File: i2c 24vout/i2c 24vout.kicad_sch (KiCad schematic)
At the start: 73 parts, among them J1 power in, J2 Conn_01x04, J3 Conn_01x04, J4 Conn_01x04, J5 Conn_01x04, J6 to qwiic breakout, U1 ILQ620GB-X009, U2 ILQ620GB-X009, U3 ILQ620GB-X009, U4 ILQ620GB-X009, U5 PCA9685PW

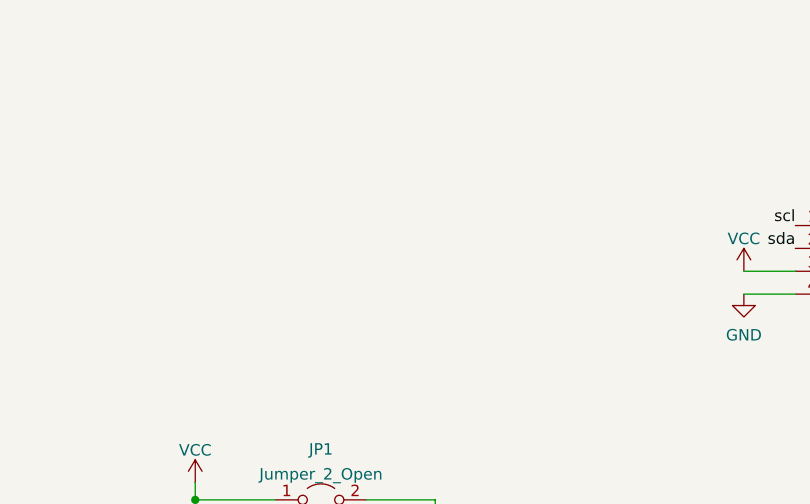
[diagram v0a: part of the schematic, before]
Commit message: added qwiic connectors to boards as well as breakout connector
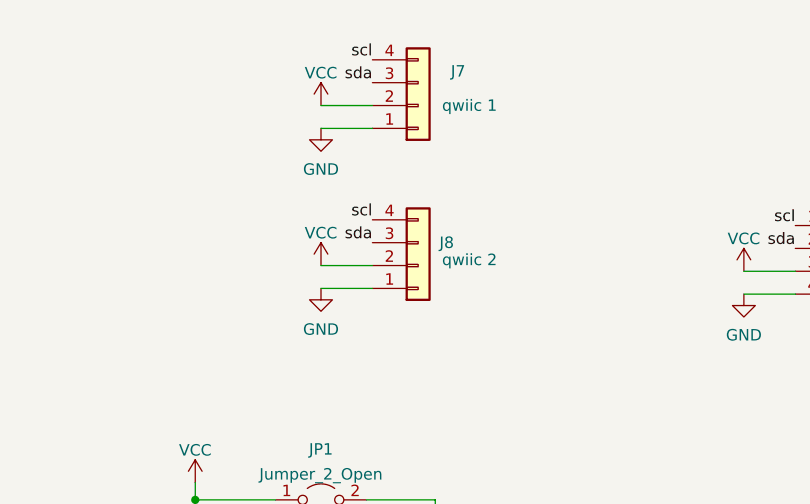
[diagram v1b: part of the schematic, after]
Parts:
- added J7: qwiic 1, Connector_JST:JST_SH_SM04B-SRSS-TB_1x04-1MP_P1.00mm_Horizontal, symbol Connector_Generic:Conn_01x04
- added J8: qwiic 2, Connector_JST:JST_SH_SM04B-SRSS-TB_1x04-1MP_P1.00mm_Horizontal, symbol Connector_Generic:Conn_01x04
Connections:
- net GND: now also J7.1 (Pin_1), J8.1 (Pin_1)
- net VCC: now also J7.2 (Pin_2), J8.2 (Pin_2)
- net scl: now also J7.4 (Pin_4), J8.4 (Pin_4)
- net sda: now also J7.3 (Pin_3), J8.3 (Pin_3)
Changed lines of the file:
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@@
+    (stroke (width 0) (type default) (color 0 0 0 0))
+  )
+  (wire (pts (xy 154.305 25.4) (xy 160.02 25.4))
     (stroke (width 0) (type default) (color 0 0 0 0))
   )
@@
     (stroke (width 0) (type default) (color 0 0 0 0))
   )
+  (wire (pts (xy 154.305 43.18) (xy 160.02 43.18))
+    (stroke (width 0) (type default) (color 0 0 0 0))
+  )
   (wire (pts (xy 60.96 79.375) (xy 71.755 79.375))
     (stroke (width 0) (type default) (color 0 0 0 0))
@@
     (stroke (width 0) (type default) (color 0 0 0 0))
   )
+  (wire (pts (xy 154.305 40.64) (xy 160.02 40.64))
+    (stroke (width 0) (type default) (color 0 0 0 0))
+  )
   (wire (pts (xy 60.96 69.215) (xy 71.755 69.215))
     (stroke (width 0) (type default) (color 0 0 0 0))
@@
   )
   (wire (pts (xy 56.515 97.155) (xy 56.515 107.315))
+    (stroke (width 0) (type default) (color 0 0 0 0))
+  )
+  (wire (pts (xy 154.305 22.86) (xy 160.02 22.86))
     (stroke (width 0) (type default) (color 0 0 0 0))
   )
@@
     (effects (font (size 1.27 1.27)) (justify right bottom))
   )
+  (label "sda" (at 160.02 20.32 180)
+    (effects (font (size 1.27 1.27)) (justify right bottom))
+  )
   (label "pwm12" (at 263.525 78.105 0)
     (effects (font (size 1.27 1.27)) (justify left bottom))
@@
     (effects (font (size 1.27 1.27)) (justify right bottom))
   )
+  (label "scl" (at 160.02 35.56 180)
+    (effects (font (size 1.27 1.27)) (justify right bottom))
+  )
   (label "pwm5" (at 23.495 76.835 180)
     (effects (font (size 1.27 1.27)) (justify right bottom))
@@
     (effects (font (size 1.27 1.27)) (justify right bottom))
   )
+  (label "sda" (at 160.02 38.1 180)
+    (effects (font (size 1.27 1.27)) (justify right bottom))
+  )
   (label "pwm14" (at 23.495 168.275 180)
     (effects (font (size 1.27 1.27)) (justify right bottom))
@@
   )
   (label "pwm1" (at 23.495 36.195 180)
+    (effects (font (size 1.27 1.27)) (justify right bottom))
+  )
+  (label "scl" (at 160.02 17.78 180)
     (effects (font (size 1.27 1.27)) (justify right bottom))
   )
@@
     (pin "3")
     (pin "4")
+  )
+  (symbol (lib_id "power:GND") (at 154.305 43.18 0) (unit 1)
+    (in_bom yes) (on_board yes) (fields_autoplaced)
+    (property "Reference" "#PWR04" (id 0) (at 154.305 49.53 0)
+      (effects (font (size 1.27 1.27)) hide)
+    )
+    (property "Value" "GND" (id 1) (at 154.305 47.7425 0))
+    (property "Footprint" "" (id 2) (at 154.305 43.18 0)
+      (effects (font (size 1.27 1.27)) hide)
+    )
+    (property "Datasheet" "" (id 3) (at 154.305 43.18 0)
+      (effects (font (size 1.27 1.27)) hide)
+    )
+    (pin "1")
   )
   (symbol (lib_id "Evan's misc parts:ILQ620GB-X009") (at 42.545 99.695 0) (unit 1)
@@
     (pin "2")
   )
+  (symbol (lib_id "power:GND") (at 154.305 25.4 0) (unit 1)
+    (in_bom yes) (on_board yes) (fields_autoplaced)
+    (property "Reference" "#PWR02" (id 0) (at 154.305 31.75 0)
+      (effects (font (size 1.27 1.27)) hide)
+    )
+    (property "Value" "GND" (id 1) (at 154.305 29.9625 0))
+    (property "Footprint" "" (id 2) (at 154.305 25.4 0)
+      (effects (font (size 1.27 1.27)) hide)
+    )
+    (property "Datasheet" "" (id 3) (at 154.305 25.4 0)
+      (effects (font (size 1.27 1.27)) hide)
+    )
+    (pin "1")
+  )
   (symbol (lib_id "Device:R") (at 27.305 26.035 270) (unit 1)
     (in_bom yes) (on_board yes) (fields_autoplaced)
@@
     (pin "2")
   )
+  (symbol (lib_id "power:VCC") (at 154.305 40.64 0) (unit 1)
+    (in_bom yes) (on_board yes) (fields_autoplaced)
+    (property "Reference" "#PWR03" (id 0) (at 154.305 44.45 0)
+      (effects (font (size 1.27 1.27)) hide)
+    )
+    (property "Value" "VCC" (id 1) (at 154.305 37.0355 0))
+    (property "Footprint" "" (id 2) (at 154.305 40.64 0)
+      (effects (font (size 1.27 1.27)) hide)
+    )
+    (property "Datasheet" "" (id 3) (at 154.305 40.64 0)
+      (effects (font (size 1.27 1.27)) hide)
+    )
+    (pin "1")
+  )
   (symbol (lib_id "Device:R") (at 27.305 66.675 270) (unit 1)
     (in_bom yes) (on_board yes) (fields_autoplaced)
@@
     (pin "1")
   )
+  (symbol (lib_id "Connector_Generic:Conn_01x04") (at 165.1 40.64 0) (mirror x) (unit 1)
+    (in_bom yes) (on_board yes)
+    (property "Reference" "J8" (id 0) (at 168.275 38.1 0))
+    (property "Value" "qwiic 2" (id 1) (at 170.815 40.005 0))
+    (property "Footprint" "Connector_JST:JST_SH_SM04B-SRSS-TB_1x04-1MP_P1.00mm_Horizontal" (id 2) (at 165.1 40.64 0)
+      (effects (font (size 1.27 1.27)) hide)
+    )
+    (property "Datasheet" "~" (id 3) (at 165.1 40.64 0)
+      (effects (font (size 1.27 1.27)) hide)
+    )
+    (pin "1")
+    (pin "2")
+    (pin "3")
+    (pin "4")
+  )
   (symbol (lib_id "power:+24V") (at 56.515 19.685 0) (unit 1)
     (in_bom yes) (on_board yes) (fields_autoplaced)
@@
     (pin "1")
     (pin "2")
+  )
+  (symbol (lib_id "power:VCC") (at 154.305 22.86 0) (unit 1)
+    (in_bom yes) (on_board yes) (fields_autoplaced)
+    (property "Reference" "#PWR01" (id 0) (at 154.305 26.67 0)
+      (effects (font (size 1.27 1.27)) hide)
+    )
+    (property "Value" "VCC" (id 1) (at 154.305 19.2555 0))
+    (property "Footprint" "" (id 2) (at 154.305 22.86 0)
+      (effects (font (size 1.27 1.27)) hide)
+    )
+    (property "Datasheet" "" (id 3) (at 154.305 22.86 0)
+      (effects (font (size 1.27 1.27)) hide)
+    )
+    (pin "1")
   )
   (symbol (lib_id "Device:C") (at 60.96 65.405 0) (unit 1)
@@
     (pin "2")
   )
+  (symbol (lib_id "Connector_Generic:Conn_01x04") (at 165.1 22.86 0) (mirror x) (unit 1)
+    (in_bom yes) (on_board yes)
+    (property "Reference" "J7" (id 0) (at 169.545 19.05 0))
+    (property "Value" "qwiic 1" (id 1) (at 170.815 22.86 0))
+    (property "Footprint" "Connector_JST:JST_SH_SM04B-SRSS-TB_1x04-1MP_P1.00mm_Horizontal" (id 2) (at 165.1 22.86 0)
+      (effects (font (size 1.27 1.27)) hide)
+    )
+    (property "Datasheet" "~" (id 3) (at 165.1 22.86 0)
+      (effects (font (size 1.27 1.27)) hide)
+    )
+    (pin "1")
+    (pin "2")
+    (pin "3")
+    (pin "4")
+  )
   (symbol (lib_id "Device:R") (at 71.755 45.085 0) (unit 1)
     (in_bom yes) (on_board yes) (fields_autoplaced)
@@
   )
   (symbol_instances
+    (path "/b71aee81-8ccc-488b-87a3-550495135d8e"
+      (reference "#PWR01") (unit 1) (value "VCC") (footprint "")
+    )
+    (path "/4175c327-a7fe-4d84-ba69-9ba6e02c58fb"
+      (reference "#PWR02") (unit 1) (value "GND") (footprint "")
+    )
+    (path "/52ec8b76-9d1a-4183-bd6e-a535fa00310c"
+      (reference "#PWR03") (unit 1) (value "VCC") (footprint "")
+    )
+    (path "/12f5ec82-4dbe-408e-aaae-0e3618d856e5"
+      (reference "#PWR04") (unit 1) (value "GND") (footprint "")
+    )
     (path "/653b3b7f-63b7-4063-8482-5cb2e6bca5d9"
       (reference "#PWR0101") (unit 1) (value "GND") (footprint "")
@@
       (reference "J6") (unit 1) (value "to qwiic breakout") (footprint "Connector_PinHeader_2.54mm:PinHeader_1x04_P2.54mm_Vertical")
     )
+    (path "/e8cfcc49-0e38-439d-bb8a-686b576038c2"
+      (reference "J7") (unit 1) (value "qwiic 1") (footprint "Connector_JST:JST_SH_SM04B-SRSS-TB_1x04-1MP_P1.00mm_Horizontal")
+    )
+    (path "/9a77615a-bb77-4b24-9f7e-2a282758ce30"
+      (reference "J8") (unit 1) (value "qwiic 2") (footprint "Connector_JST:JST_SH_SM04B-SRSS-TB_1x04-1MP_P1.00mm_Horizontal")
+    )
     (path "/f620a1b7-aab5-4053-912e-f514c747583a"

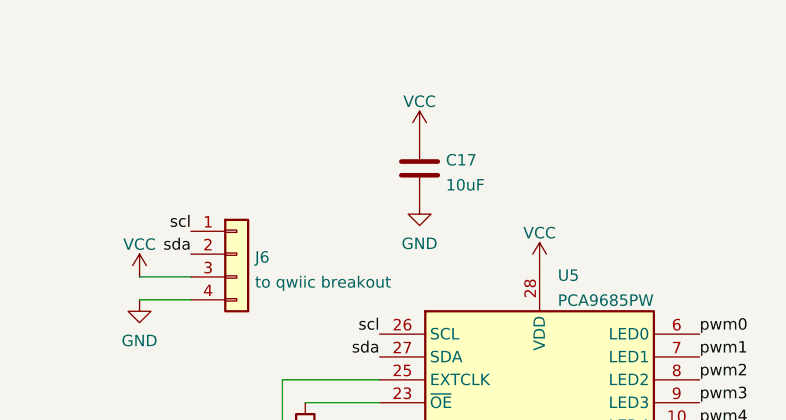
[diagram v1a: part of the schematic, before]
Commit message: reel detent added
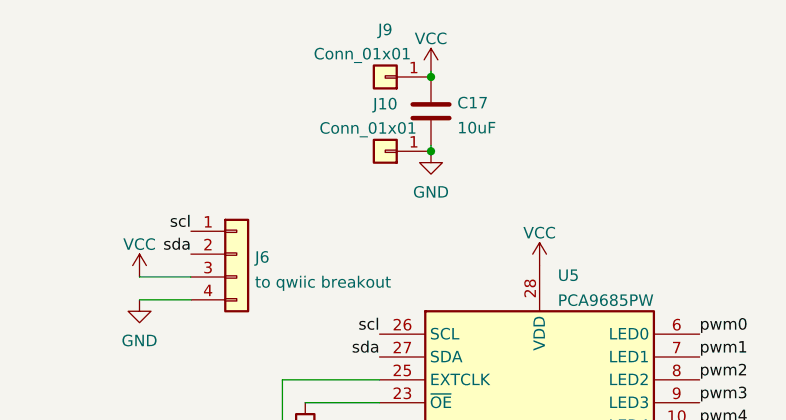
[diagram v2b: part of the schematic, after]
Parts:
- added J10, J9: Conn_01x01, Connector_PinHeader_2.54mm:PinHeader_1x01_P2.54mm_Vertical, symbol Connector_Generic:Conn_01x01
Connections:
- net GND: now also J10.1 (Pin_1)
- net VCC: now also J9.1 (Pin_1)
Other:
- moved on the sheet: C17
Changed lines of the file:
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@@
   (junction (at 33.02 41.275) (diameter 0) (color 0 0 0 0)
   )
+  (junction (at 233.68 27.305) (diameter 0) (color 0 0 0 0)
+  )
   (junction (at 78.105 150.495) (diameter 0) (color 0 0 0 0)
   )
@@
   (junction (at 187.96 121.285) (diameter 0) (color 0 0 0 0)
   )
+  (junction (at 233.68 19.05) (diameter 0) (color 0 0 0 0)
+  )
   (junction (at 56.515 168.275) (diameter 0) (color 0 0 0 0)
   )
@@
     (stroke (width 0) (type default) (color 0 0 0 0))
   )
+  (wire (pts (xy 233.68 27.305) (xy 233.68 26.67))
+    (stroke (width 0) (type default) (color 0 0 0 0))
+  )
   (wire (pts (xy 71.755 150.495) (xy 78.105 150.495))
     (stroke (width 0) (type default) (color 0 0 0 0))
@@
   )
   (wire (pts (xy 159.385 92.71) (xy 187.96 92.71))
+    (stroke (width 0) (type default) (color 0 0 0 0))
+  )
+  (wire (pts (xy 233.68 18.415) (xy 233.68 19.05))
     (stroke (width 0) (type default) (color 0 0 0 0))
   )
@@
     (pin "16")
     (pin "2")
+  )
+  (symbol (lib_id "Connector_Generic:Conn_01x01") (at 228.6 27.305 180) (unit 1)
+    (in_bom yes) (on_board yes)
+    (property "Reference" "J10" (id 0) (at 228.6 22.0685 0))
+    (property "Value" "Conn_01x01" (id 1) (at 226.695 24.765 0))
+    (property "Footprint" "Connector_PinHeader_2.54mm:PinHeader_1x01_P2.54mm_Vertical" (id 2) (at 228.6 27.305 0)
+      (effects (font (size 1.27 1.27)) hide)
+    )
+    (property "Datasheet" "~" (id 3) (at 228.6 27.305 0)
+      (effects (font (size 1.27 1.27)) hide)
+    )
+    (pin "1")
   )
   (symbol (lib_id "Device:R") (at 27.305 86.995 270) (unit 1)
@@
     (pin "1")
   )
-  (symbol (lib_id "power:VCC") (at 232.41 25.4 0) (unit 1)
-    (in_bom yes) (on_board yes) (fields_autoplaced)
-    (property "Reference" "#PWR0112" (id 0) (at 232.41 29.21 0)
-      (effects (font (size 1.27 1.27)) hide)
-    )
-    (property "Value" "VCC" (id 1) (at 232.41 21.7955 0))
-    (property "Footprint" "" (id 2) (at 232.41 25.4 0)
-      (effects (font (size 1.27 1.27)) hide)
-    )
-    (property "Datasheet" "" (id 3) (at 232.41 25.4 0)
+  (symbol (lib_id "power:VCC") (at 233.68 18.415 0) (unit 1)
+    (in_bom yes) (on_board yes) (fields_autoplaced)
+    (property "Reference" "#PWR0112" (id 0) (at 233.68 22.225 0)
+      (effects (font (size 1.27 1.27)) hide)
+    )
+    (property "Value" "VCC" (id 1) (at 233.68 14.8105 0))
+    (property "Footprint" "" (id 2) (at 233.68 18.415 0)
+      (effects (font (size 1.27 1.27)) hide)
+    )
+    (property "Datasheet" "" (id 3) (at 233.68 18.415 0)
       (effects (font (size 1.27 1.27)) hide)
     )
@@
     (pin "2")
   )
-  (symbol (lib_id "Device:C") (at 232.41 29.21 0) (unit 1)
-    (in_bom yes) (on_board yes) (fields_autoplaced)
-    (property "Reference" "C17" (id 0) (at 235.331 28.3015 0)
-      (effects (font (size 1.27 1.27)) (justify left))
-    )
-    (property "Value" "10uF" (id 1) (at 235.331 31.0766 0)
-      (effects (font (size 1.27 1.27)) (justify left))
-    )
-    (property "Footprint" "Capacitor_SMD:C_0603_1608Metric" (id 2) (at 233.3752 33.02 0)
-      (effects (font (size 1.27 1.27)) hide)
-    )
-    (property "Datasheet" "~" (id 3) (at 232.41 29.21 0)
+  (symbol (lib_id "Device:C") (at 233.68 22.86 0) (unit 1)
+    (in_bom yes) (on_board yes) (fields_autoplaced)
+    (property "Reference" "C17" (id 0) (at 236.601 21.9515 0)
+      (effects (font (size 1.27 1.27)) (justify left))
+    )
+    (property "Value" "10uF" (id 1) (at 236.601 24.7266 0)
+      (effects (font (size 1.27 1.27)) (justify left))
+    )
+    (property "Footprint" "Capacitor_SMD:C_0603_1608Metric" (id 2) (at 234.6452 26.67 0)
+      (effects (font (size 1.27 1.27)) hide)
+    )
+    (property "Datasheet" "~" (id 3) (at 233.68 22.86 0)
       (effects (font (size 1.27 1.27)) hide)
     )
@@
     (pin "2")
   )
+  (symbol (lib_id "Connector_Generic:Conn_01x01") (at 228.6 19.05 180) (unit 1)
+    (in_bom yes) (on_board yes)
+    (property "Reference" "J9" (id 0) (at 228.6 13.8135 0))
+    (property "Value" "Conn_01x01" (id 1) (at 226.06 16.51 0))
+    (property "Footprint" "Connector_PinHeader_2.54mm:PinHeader_1x01_P2.54mm_Vertical" (id 2) (at 228.6 19.05 0)
+      (effects (font (size 1.27 1.27)) hide)
+    )
+    (property "Datasheet" "~" (id 3) (at 228.6 19.05 0)
+      (effects (font (size 1.27 1.27)) hide)
+    )
+    (pin "1")
+  )
   (symbol (lib_id "power:VCC") (at 245.745 40.005 0) (unit 1)
     (in_bom yes) (on_board yes) (fields_autoplaced)
@@
     (pin "9")
   )
-  (symbol (lib_id "power:GND") (at 232.41 33.02 0) (unit 1)
-    (in_bom yes) (on_board yes) (fields_autoplaced)
-    (property "Reference" "#PWR0113" (id 0) (at 232.41 39.37 0)
-      (effects (font (size 1.27 1.27)) hide)
-    )
-    (property "Value" "GND" (id 1) (at 232.41 37.5825 0))
-    (property "Footprint" "" (id 2) (at 232.41 33.02 0)
-      (effects (font (size 1.27 1.27)) hide)
-    )
-    (property "Datasheet" "" (id 3) (at 232.41 33.02 0)
+  (symbol (lib_id "power:GND") (at 233.68 27.305 0) (unit 1)
+    (in_bom yes) (on_board yes) (fields_autoplaced)
+    (property "Reference" "#PWR0113" (id 0) (at 233.68 33.655 0)
+      (effects (font (size 1.27 1.27)) hide)
+    )
+    (property "Value" "GND" (id 1) (at 233.68 31.8675 0))
+    (property "Footprint" "" (id 2) (at 233.68 27.305 0)
+      (effects (font (size 1.27 1.27)) hide)
+    )
+    (property "Datasheet" "" (id 3) (at 233.68 27.305 0)
       (effects (font (size 1.27 1.27)) hide)
     )
@@
       (reference "J8") (unit 1) (value "qwiic 2") (footprint "Connector_JST:JST_SH_SM04B-SRSS-TB_1x04-1MP_P1.00mm_Horizontal")
     )
+    (path "/c3bdf5ca-ea70-4125-9fd7-38a5f634fb76"
+      (reference "J9") (unit 1) (value "Conn_01x01") (footprint "Connector_PinHeader_2.54mm:PinHeader_1x01_P2.54mm_Vertical")
+    )
+    (path "/1b9d142d-e7df-431e-a51b-09e10f8ea9c8"
+      (reference "J10") (unit 1) (value "Conn_01x01") (footprint "Connector_PinHeader_2.54mm:PinHeader_1x01_P2.54mm_Vertical")
+    )
     (path "/f620a1b7-aab5-4053-912e-f514c747583a"

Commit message: lots of stuff, I don't even know
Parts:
- added R40, R41, R42, R43, R44, R45, R46, R47, R48, R49, R50, R51, R52, R53, R54, R55: 0, Resistor_SMD:R_0603_1608Metric, symbol Device:R
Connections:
- net at C7.1, R23.1, U2.13: now also R46.1; no longer J3.3 (Pin_3)
- net at C13.1, R29.1, U4.9: now also R52.1; no longer J5.1 (Pin_1)
- net at C14.1, R30.1, U4.11: now also R53.1; no longer J5.2 (Pin_2)
- net at C15.1, R31.1, U4.13: now also R54.1; no longer J5.3 (Pin_3)
- net at C16.1, R32.1, U4.15: now also R55.1; no longer J5.4 (Pin_4)
- net at C10.1, R26.1, U3.11: now also R49.1; no longer J4.2 (Pin_2)
- net at C3.1, R19.1, U1.13: now also R42.1; no longer J2.3 (Pin_3)
- net at C8.1, R24.1, U2.15: now also R47.1; no longer J3.4 (Pin_4)
- net at C5.1, R21.1, U2.9: now also R44.1; no longer J3.1 (Pin_1)
- net at C4.1, R20.1, U1.15: now also R43.1; no longer J2.4 (Pin_4)
- net at C11.1, R27.1, U3.13: now also R50.1; no longer J4.3 (Pin_3)
- net at C9.1, R25.1, U3.9: now also R48.1; no longer J4.1 (Pin_1)
- net at C6.1, R22.1, U2.11: now also R45.1; no longer J3.2 (Pin_2)
- net at C12.1, R28.1, U3.15: now also R51.1; no longer J4.4 (Pin_4)
- net at C2.1, R18.1, U1.11: now also R41.1; no longer J2.2 (Pin_2)
- net at C1.1, R17.1, U1.9: now also R40.1; no longer J2.1 (Pin_1)
- new net: J2.3 (Pin_3), R42.2
- new net: J5.1 (Pin_1), R52.2
- new net: J5.2 (Pin_2), R53.2
- new net: J5.3 (Pin_3), R54.2
- new net: J5.4 (Pin_4), R55.2
- new net: J4.4 (Pin_4), R51.2
- new net: J3.4 (Pin_4), R47.2
- new net: J4.3 (Pin_3), R50.2
- new net: J3.2 (Pin_2), R45.2
- new net: J2.2 (Pin_2), R41.2
- new net: J2.1 (Pin_1), R40.2
- new net: J4.2 (Pin_2), R49.2
- new net: J4.1 (Pin_1), R48.2
- new net: J3.1 (Pin_1), R44.2
- new net: J3.3 (Pin_3), R46.2
- new net: J2.4 (Pin_4), R43.2
